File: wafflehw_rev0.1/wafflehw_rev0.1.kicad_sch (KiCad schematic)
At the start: 38 parts, among them J1 USB_C_Receptacle_USB2.0_14P, J2 OLED_Disp, J3 FH34SRJ-30S-0.5SH, J4 BATT, J5 LCD_BL, M1 Motor_DC, Q1 2N7002K, Q2 2N7002H, Q3 2N7002H, SW1 SW_Push, SW2 BTN_UP, SW3 BTN_DN, SW4 BTN_OK, U1 Ai-Thinker-Ra-01, U2 MCP73831-2-OT, U3 ESP32-S3-WROOM-1, U4 MIC5219-3.3YM5

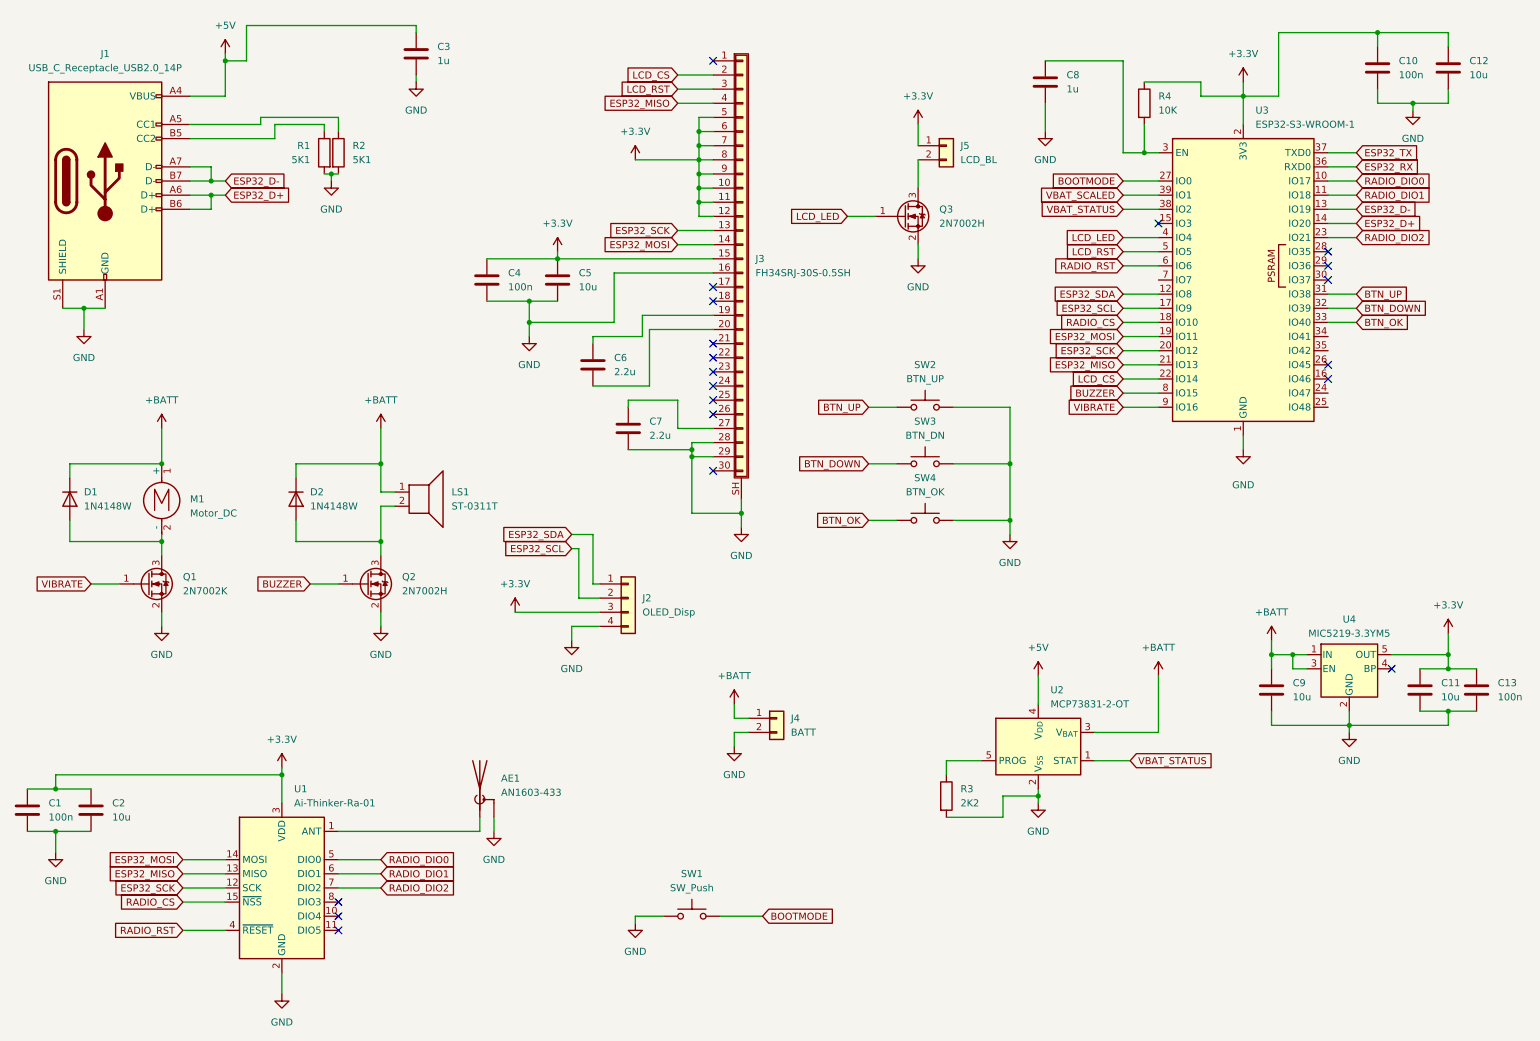
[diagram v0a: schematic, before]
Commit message: Schematic improvements
- Changed to two LDOs and add ferrite beads
- Changed battery charging IC to pin compatible TP4054
- USB connector changed to more common variant
- Antenna pad disconnected from ground
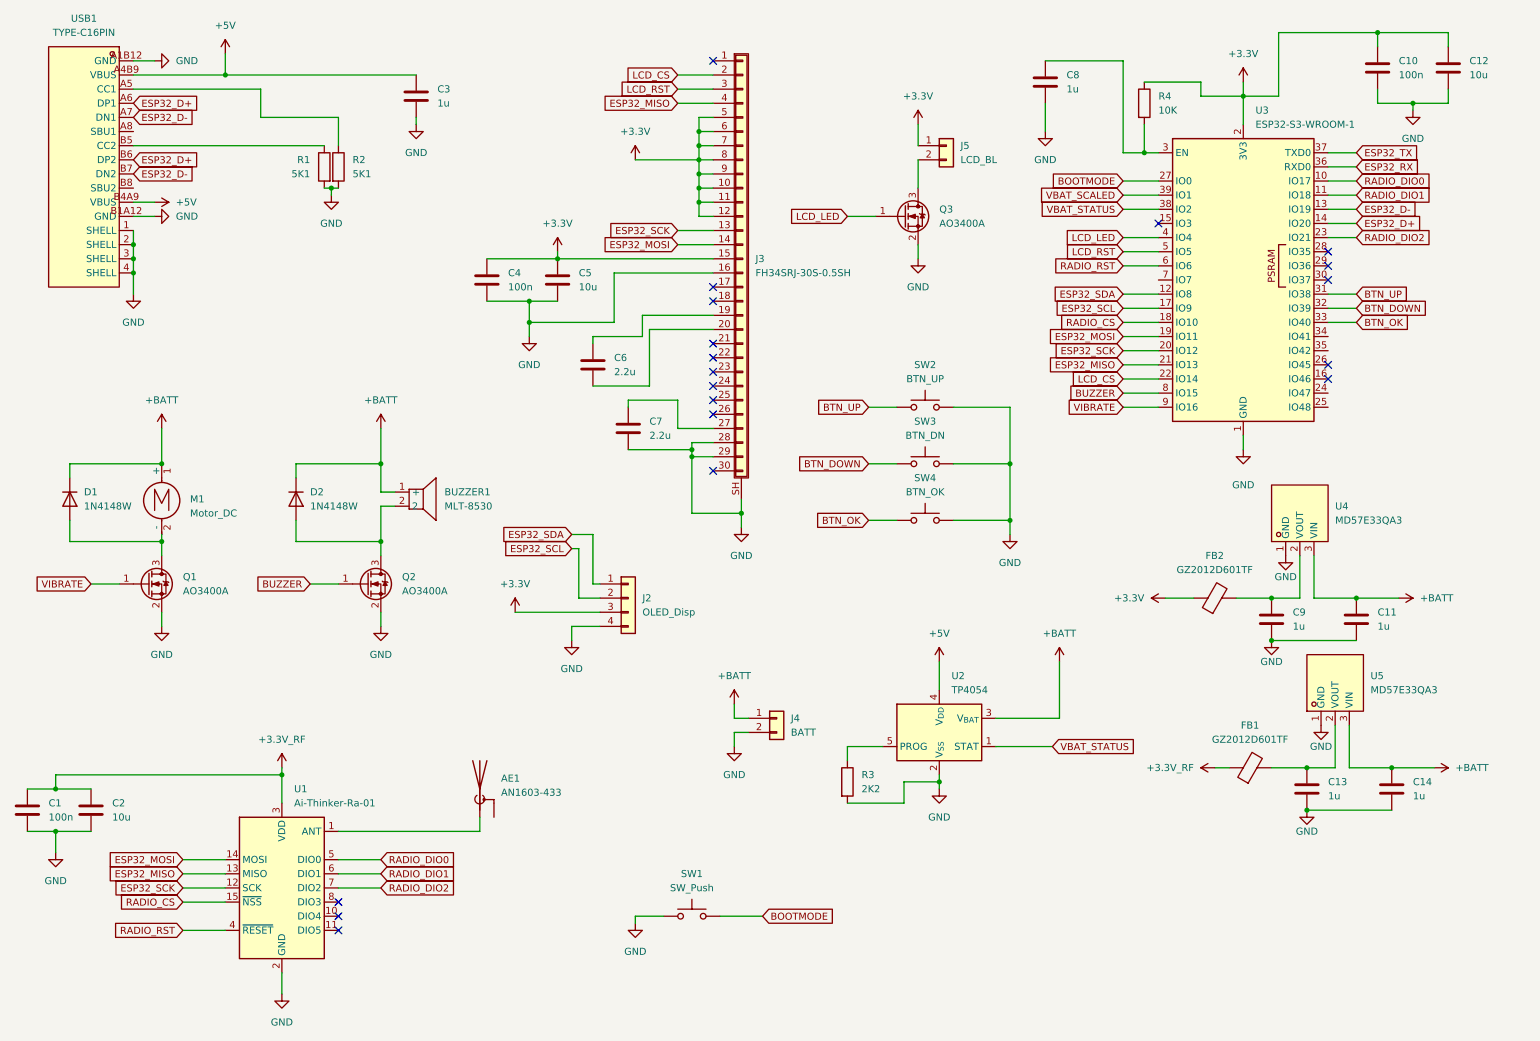
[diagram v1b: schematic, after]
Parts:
- removed J1: USB_C_Receptacle_USB2.0_14P, Connector_USB:USB_C_Receptacle_GCT_USB4085, symbol Connector:USB_C_Receptacle_USB2.0_14P
- removed LS1: ST-0311T, Waffle2Rev0.1:ST-0311T, symbol Device:Speaker
- removed Q1: 2N7002K, Package_TO_SOT_SMD:SOT-23, symbol Transistor_FET:2N7002K
- removed Q2, Q3: 2N7002H, Package_TO_SOT_SMD:SOT-23, symbol Transistor_FET:2N7002H
- removed U4: MIC5219-3.3YM5, Package_TO_SOT_SMD:SOT-23-5, symbol Regulator_Linear:MIC5219-3.3YM5
- added BUZZER1: MLT-8530, easyeda:BUZ-SMD_4P-L8.5-W8.5-P8.50-BR, symbol easyeda:MLT-8530
- added C14: 1u, Capacitor_SMD:C_0805_2012Metric, symbol Device:C
- added FB1, FB2: GZ2012D601TF, Inductor_SMD:L_0805_2012Metric, symbol Device:FerriteBead
- added Q1, Q2, Q3: AO3400A, Package_TO_SOT_SMD:SOT-23, symbol Transistor_FET:AO3400A
- added U4, U5: MD57E33QA3, easyeda:SOT-23-3_L2.9-W1.6-P1.90-LS2.8-BR, symbol easyeda:MD57E33QA3
- added USB1: TYPE-C16PIN, easyeda:USB-C-SMD_TYPE-C16PIN, symbol easyeda:TYPE-C16PIN
- C11, C9: value 10u -> 1u
- C13: value 100n -> 1u
- U2: value MCP73831-2-OT -> TP4054
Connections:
- net +3.3V: now also FB2.1; no longer C1.1, C11.1, C13.1, C2.1, U1.3 (VDD)
- net +5V: now also USB1.A4B9 (VBUS), USB1.B4A9 (VBUS)
- net +BATT: now also C11.1, BUZZER1.1 (+), C14.1, U4.3 (VIN), U5.3 (VIN); no longer C9.1
- net BUZZER: now also Q2.1 (G)
- net ESP32_D+: now also USB1.A6 (DP1), USB1.B6 (DP2)
- net ESP32_D-: now also USB1.A7 (DN1), USB1.B7 (DN2)
- net GND: now also C14.2, Q1.2 (S), Q2.2 (S), Q3.2 (S), U4.1 (GND), U5.1 (GND), USB1.1 (SHELL), USB1.2 (SHELL), USB1.3 (SHELL), USB1.4 (SHELL), USB1.A1B12 (GND), USB1.B1A12 (GND); no longer AE1.2 (Shield)
- net LCD_LED: now also Q3.1 (G)
- net VIBRATE: now also Q1.1 (G)
- net at J5.2 (Pin_2): now also Q3.3 (D)
- net at R2.1: now also USB1.A5 (CC1)
- net at D1.2 (A), M1.2 (-): now also Q1.3 (D)
- net at D2.2 (A): now also BUZZER1.2, Q2.3 (D)
- net at R1.1: now also USB1.B5 (CC2)
- new net: C9.1, FB2.2, U4.2 (VOUT)
- new net: C13.1, FB1.2, U5.2 (VOUT)
- new net +3.3V_RF: C1.1, C2.1, FB1.1, U1.3 (VDD)
- no-connect marks 20 -> 19
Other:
- moved on the sheet: C3, R1, R2, R3, U2
